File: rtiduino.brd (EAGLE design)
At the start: 181.8 x 126 mm, 111 parts, among them IC7 LM358D, J1 DCJ0202, J2 3.5MM-JACK, J3 2.5MM-JACK, Q2 16MHz, T1 NDT2955, T2 FDN340P, U1 ATMEGA2560AU, U10 AQV252G, U11 AQV252G, U12 AQV252G, U13 AQV252G, U14 AQV252G, U15 AQV252G, U16 AQV252G, U17 AQV252G, U2 LDU240S500, U20 AQV252G, U21 AQV252G, U22 AQV252G, U23 AQV252G, U24 AQV252G, U25 AQV252G, U26 AQV252G, U27 AQV252G, U3 LM2594HVM-3.3, U30 AQV252G, U31 AQV252G, U32 AQV252G, U33 AQV252G, U34 AQV252G, U35 AQV252G, U36 AQV252G, U37 AQV252G, U4 FT232RL, U5 FOD852

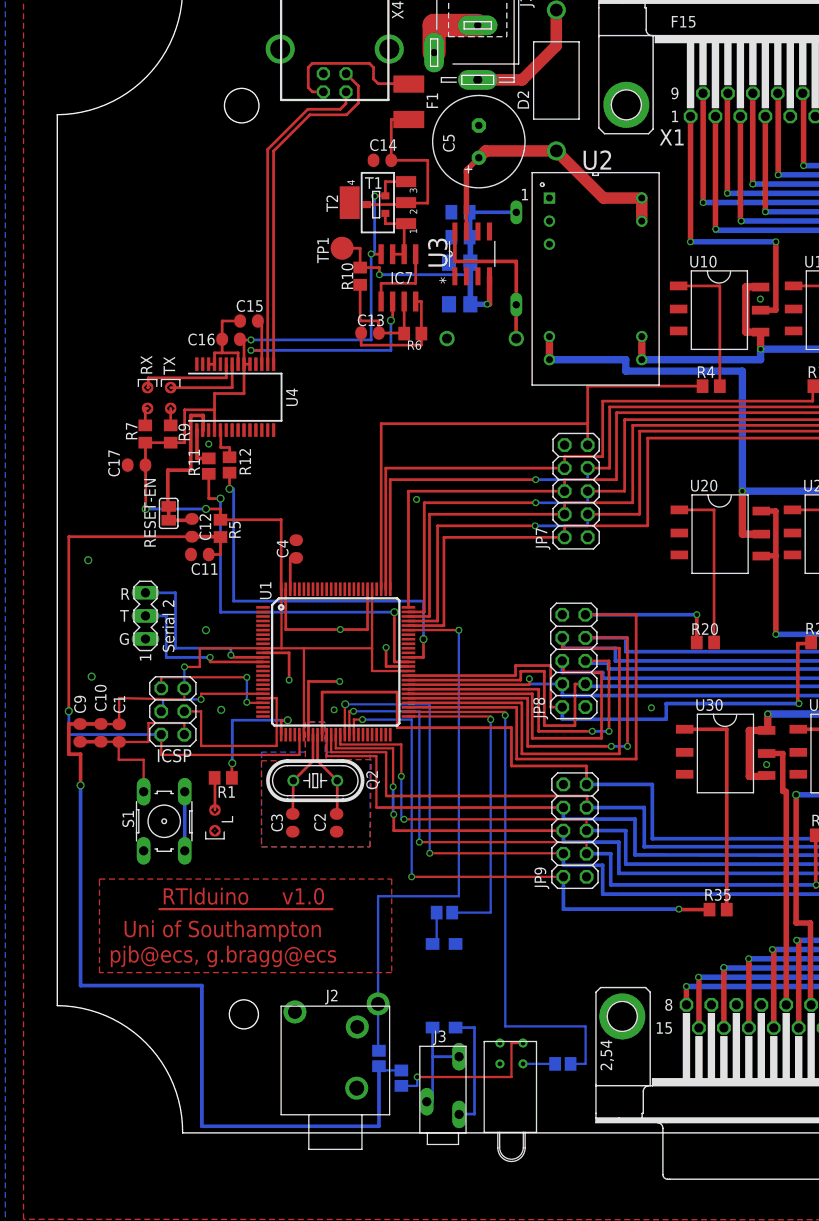
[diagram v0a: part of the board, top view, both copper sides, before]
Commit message: Latest version with * fixed PSU arrangement * more caps * connectors moved outwards
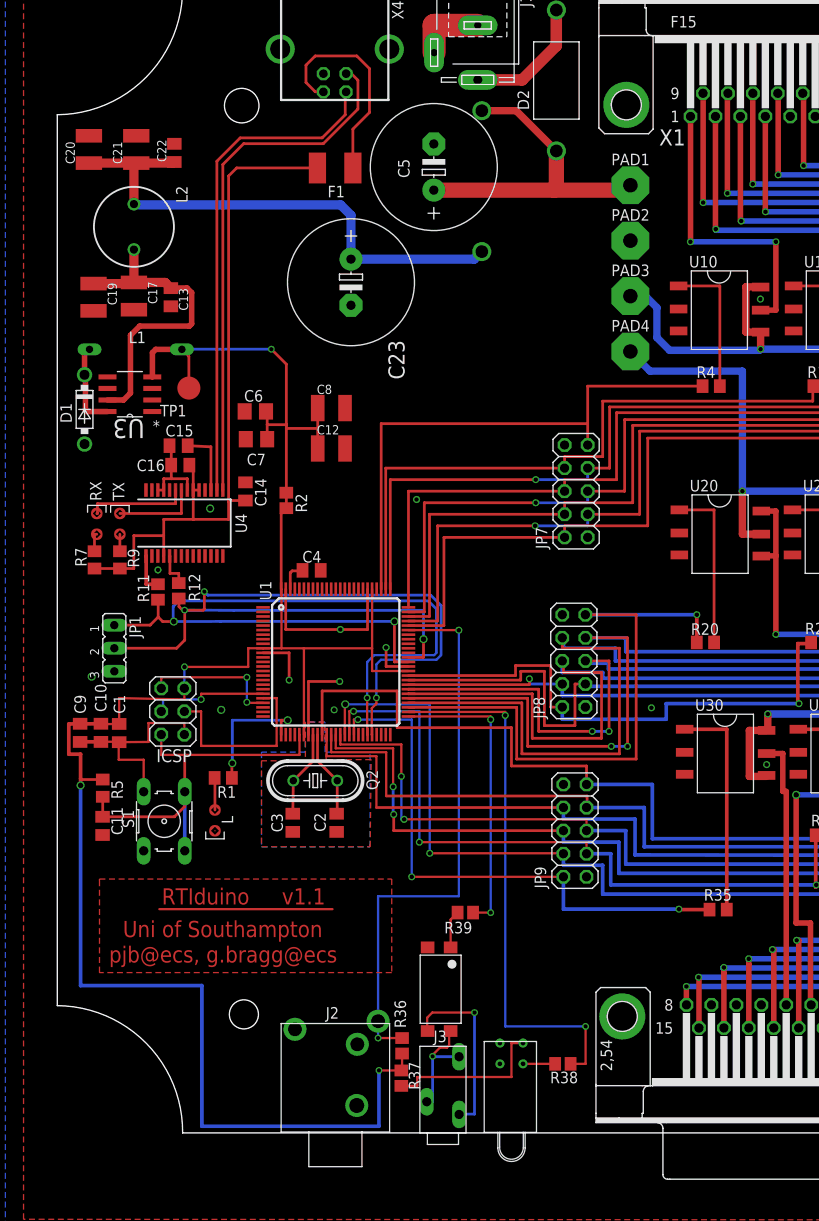
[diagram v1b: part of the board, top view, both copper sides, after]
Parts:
- removed C18: (no value), resistor:C0805K
- removed IC7: LM358D, linear:SO08
- removed R10, R6: 10k, rcl:R0805
- removed RESET-EN: (no value), jumper:SJ
- removed SV1: (no value), con-lstb:MA03-1
- removed T1: NDT2955, zetex:SOT223
- removed T2: FDN340P, zetex:SOT-23
- removed U2: LDU240S500, RTI:RELAY_LDU2430S700
- added C19, C20, C21: (no value), resistor:C1210K
- added C22: (no value), rcl:C0805K
- added C23: 68uF, rcl:E5-13
- added D3: SF37, farnell-parts:DO-201AD
- added JP1: (no value), jumper:JP2
- added L2: (no value), rcl:6000-XXXX-RC
- added PAD1: VIN, wirepad:4,16O1,6
- added PAD2: GND, wirepad:4,16O1,6
- added PAD3: LED_VCC, wirepad:4,16O1,6
- added PAD4: LED_GND, wirepad:4,16O1,6
- added R2: 0R, resistor:R0805
- C1, C10, C11, C14, C15, C16, C2, C3, C4, C9: device rcl:C0805RND -> rcl:C0805K
- C12, C17: value 100n -> (none); device rcl:C0805RND -> resistor:C1210K
- C13: value 100n -> (none); device rcl:C0805RND -> rcl:C0805K
- C5: device resistor:E3,5-10 -> rcl:E5-13
- C8: device resistor:C0805K -> resistor:C1210K
- moved D1 44.4 mm to (3.71, 78.1), flipped to the top, turned to 270 degrees
- moved L1 43.0 mm to (9.34, 84.7), turned to 180 degrees
- moved U3 40.7 mm to (8.70, 79.8), turned to 180 degrees
- moved C14 39.4 mm to (21.4, 69.1), turned to 90 degrees
- moved C11 31.7 mm to (5.69, 32.3), turned to 270 degrees
- moved R5 31.4 mm to (5.71, 36.4)
- moved C7 29.6 mm to (22.6, 74.8), flipped to the top, turned to 0 degrees
- moved C6 25.4 mm to (22.5, 77.9), flipped to the top, turned to 0 degrees
- moved C8 23.6 mm to (30.9, 78.2), flipped to the top
- moved TP1 22.8 mm to (15.2, 80.4), turned to 90 degrees
- moved C13 22.3 mm to (13.2, 90.4), turned to 270 degrees
- moved C17 18.6 mm to (9.14, 90.6), turned to 270 degrees
- moved C12 17.6 mm to (30.9, 73.8), turned to 0 degrees
- moved C15 15.8 mm to (14.1, 74.1)
- moved C16 14.9 mm to (14.2, 72.0)
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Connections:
- removed net 5VREG: C18.1, C6.+, C7.+, C8.1, L1.2, R10.2, TP1.TP, U3.4
- removed net CMP: C13.2, IC7.3, R10.1, R6.2
- removed net DTR: C12.1, RESET-EN.1, RESET-EN.2, U4.2
- removed net GATE_CMD: IC7.6, IC7.7, T1.1, T2.3
- removed net RXD3: R11.2, U1.63
- removed net TXD3: R12.2, U1.64
- new net RXD: JP1.1, R11.2, U1.45, U1.63
- new net TXD: JP1.2, R12.2, U1.46, U1.64
- net +3V3: no longer IC7.2
- net +5V: now also C12.1, C6.+, C7.+, C8.1, L1.2, R2.1, R2.2, TP1.TP, U3.4; no longer C16.1, C17.2, IC7.8, R7.2, R9.2, T1.3, T2.2, U4.19, U4.20, U4.4
- net GND: now also C12.2, C13.2, C17.2, C19.2, C20.2, C21.2, C22.2, C23.-, JP1.3, PAD2.1; no longer C13.1, C17.1, C18.2, IC7.4, R6.1, SV1.1, U2.1, U2.2
- net LED_GND: now also PAD4.1; no longer U2.7, U2.8
- net LED_VCC: now also PAD3.1; no longer U2.10, U2.9
- net N$4: now also C20.1, C21.1, C22.1, C23.+, D3.1, L2.1; no longer IC7.1, IC7.5
- net N$43: now also C13.1, C17.1, C19.1, L2.2, U3.7; no longer S1.3, S1.4
- net RESET: now also S1.3, S1.4; no longer C12.2
- net RXD2: no longer SV1.3
- net TXD2: no longer SV1.2
- net USBVCC: now also C16.1, R7.2, R9.2, U4.19, U4.20, U4.4; no longer T1.2, T2.1
- net VIN: now also D3.2, PAD1.1; no longer U2.15, U2.16, U3.7
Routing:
- net TXD: track 0.00 -> 98.0 mm, vias 0 -> 4
- net RXD: track 0.00 -> 91.4 mm, vias 0 -> 3
- net USBVCC: track 21.9 -> 79.3 mm
- net N$4: track 9.01 -> 58.0 mm
- net TXD3: track 43.3 -> 0.00 mm, vias 2 -> 0
- net RXD3: track 42.7 -> 0.00 mm, vias 2 -> 0
- net 5VREG: track 37.9 -> 0.00 mm, vias 2 -> 0
- net +5V: track 251.9 -> 223.2 mm, vias 7 -> 4
- net N$43: track 6.50 -> 34.8 mm
- net RESET: track 71.6 -> 43.6 mm, vias 1 -> 0
- net RXD2: track 20.0 -> 0.00 mm, vias 1 -> 0
- net +3V3: track 27.3 -> 7.32 mm, vias 2 -> 0
- net DTR: track 19.9 -> 0.00 mm
- net D-: track 35.6 -> 55.0 mm
- net D+: track 38.7 -> 58.0 mm
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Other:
- board text added: "v1.1"
- board text removed: "G"
- board text removed: "R"
- board text removed: "Serial 2"
- board text removed: "T"
- board text removed: "v1.0"

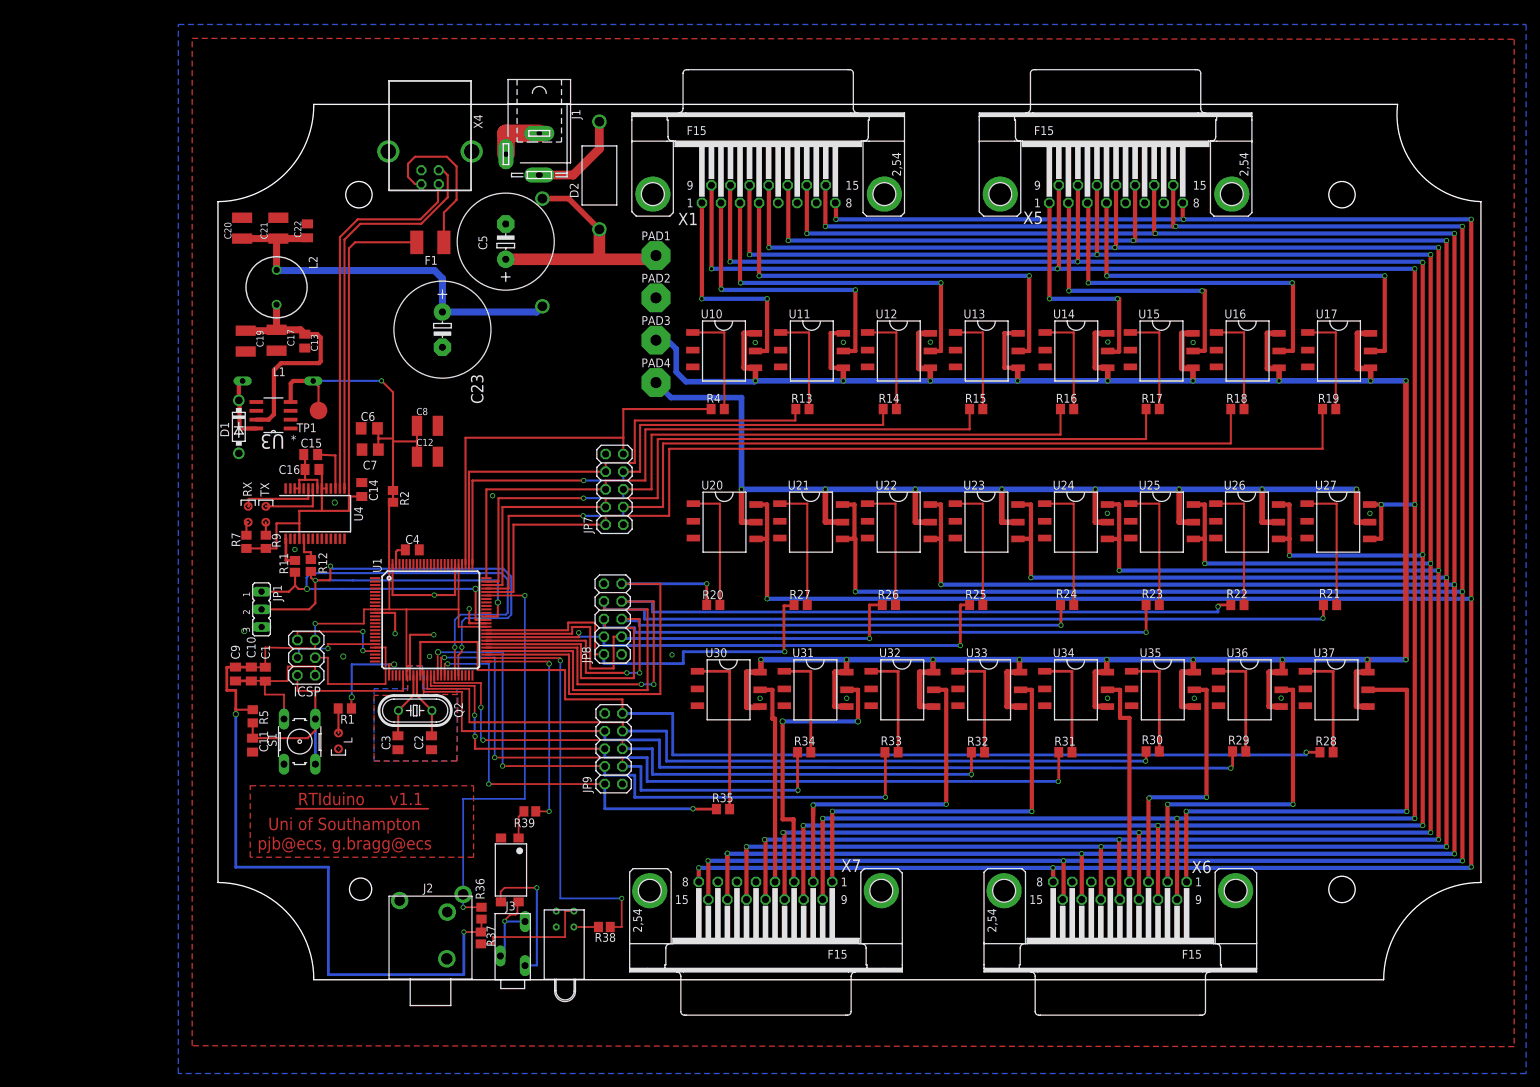
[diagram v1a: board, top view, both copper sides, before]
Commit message: Update wih Superdome PCB
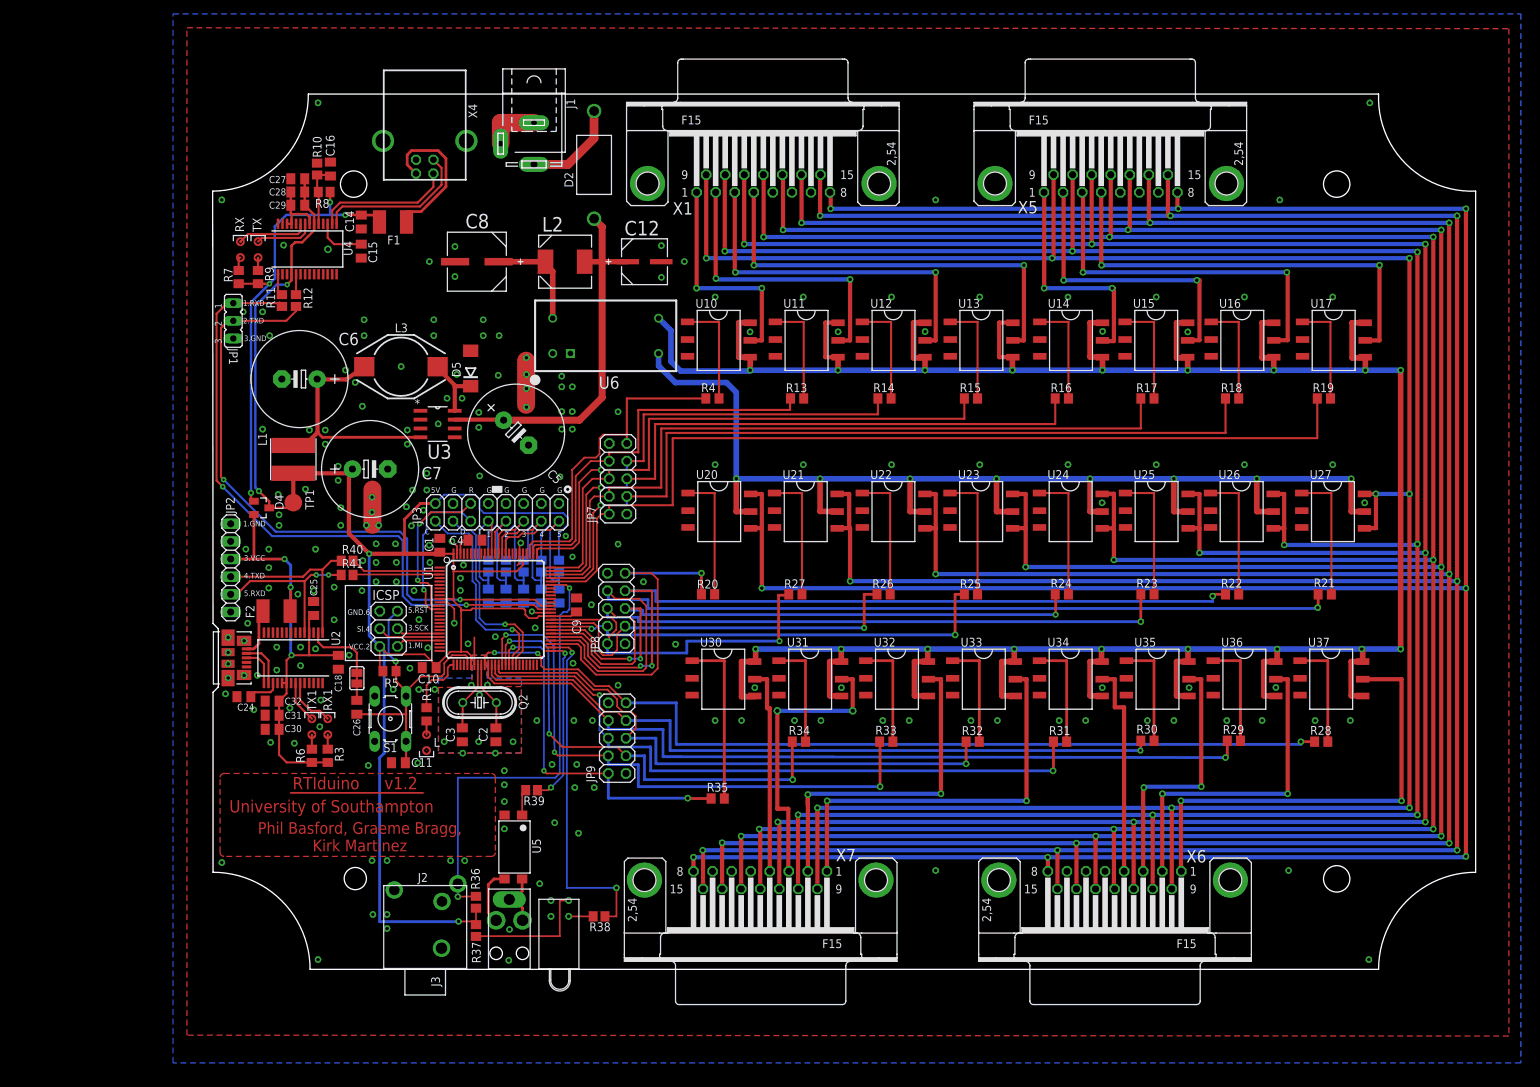
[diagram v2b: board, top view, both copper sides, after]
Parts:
- removed C13, C22: (no value), rcl:C0805K
- removed C17, C19, C20, C21: (no value), resistor:C1210K
- removed C23: 68uF, rcl:E5-13
- removed D1: 1N5817-B, diode:DO41-7.6
- removed D3: SF37, farnell-parts:DO-201AD
- removed PAD1: VIN, wirepad:4,16O1,6
- removed PAD2: GND, wirepad:4,16O1,6
- removed PAD3: LED_VCC, wirepad:4,16O1,6
- removed PAD4: LED_GND, wirepad:4,16O1,6
- removed R2: 0R, resistor:R0805
- added C18, C24, C25, C26, C27, C28, C30, C31: 100nF, rcl:C0805K
- added C29, C32: 4.7uF, rcl:C0805K
- added C42, C43, C44, C45, C46: 100n, rcl:C0805K
- added D4: BAT54C, diode:SOT23
- added D5: MBRS130, diode:DO214AA
- added F2: 500mA, rcl:L1812
- added J4: USB PROG, CC11x:MOLEX_47346-0001
- added JP2: (no value), pinhead:1X06
- added JP3: (no value), pinhead:2X08
- added L3: 330uH (DO3308P-334), inductor-coilcraft:DO3316P
- added R10: 10K, resistor:R0805
- added R3, R6: 1k, rcl:R0805
- added R40, R41: 1K, resistor:R0805
- added R42, R43, R44, R45, R46: 10k, resistor:R0805
- added R8: 4K7, resistor:R0805
- added RESET-EN: (no value), jumper:SJ
- added RX1, TX1: (no value), led:0805RND
- added U2: FT232RL, SmartPrj:SSOP28
- added U6: LED-DRIVER, RTI:LDU08
- C12: value (none) -> 10UF; device resistor:C1210K -> RTI:CAPAE660X610N
- C6: device resistor:R/2012-12R -> rcl:E5-13
- C7: value 68uF -> 100uF; device resistor:R/2012-12R -> rcl:E5-13
- C8: value (none) -> 47UF; device resistor:C1210K -> RTI:CAPAE830X1050N
- J3: value 2.5MM-JACK -> 2.5MM-JACKPRO; device RTI:2.5-JACK-RA -> RTI:2.5-JACK-RA-PRO
- L1: value 100uH -> 3uH; device inductors:SBC10 -> RTI:WE-TPC_5818/5828
- L2: value (none) -> DR73-680-R; device rcl:6000-XXXX-RC -> RTI:INDM7676X355N
- U3: value LM2594HVM-3.3 -> LM2594HVM-5.0
- moved C9 50.1 mm to (52.3, 52.5), turned to 90 degrees
- moved C16 43.3 mm to (16.9, 115.2), turned to 270 degrees
- moved C12 42.0 mm to (62.1, 101.9)
- moved JP1 41.7 mm to (2.92, 93.3)
- moved L2 41.7 mm to (50.7, 101.9), turned to 0 degrees
- moved C14 38.5 mm to (21.3, 107.6), turned to 270 degrees
- moved R11 38.3 mm to (9.91, 96.3)
- moved R12 38.2 mm to (11.9, 96.3)
- moved RX 38.1 mm to (3.94, 103.6)
- moved TX 38.1 mm to (6.48, 103.6)
- moved U4 38.1 mm to (13.6, 103.7)
- moved R7 38.1 mm to (3.69, 99.6)
- moved R9 38.1 mm to (6.48, 99.6)
- moved C1 31.2 mm to (32.6, 61.0), turned to 90 degrees
- moved C15 30.2 mm to (21.3, 103.4), turned to 90 degrees
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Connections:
- new net +3V3PROG: C24.2, U2.17
- new net N$50: RX1.P$2, U2.23
- new net N$52: TX1.P$2, U2.22
- new net N$58: R3.1, RX1.P$1
- new net N$62: R6.1, TX1.P$1
- new net N$63: F2.2, J4.1
- new net N$66: C26.1, RESET-EN.1, RESET-EN.2, U2.2
- new net N$68: C16.2, R10.1, R8.2, U4.19
- new net PROG_D+: J4.3, U2.15
- new net PROG_D-: J4.2, U2.16
- new net RXD1: U1.45
- new net RXDP: JP2.4, R40.1, U2.1
- new net RXD_PROG: R40.2, U1.2
- new net SCL: JP3.1, U1.43
- new net SDA: JP3.3, U1.44
- new net SW1: C46.1, JP3.7, R46.2, U1.89
- new net SW2: C45.1, JP3.9, R45.2, U1.88
- new net SW3: C44.1, JP3.11, R44.2, U1.87
- new net SW4: C43.1, JP3.13, R43.2, U1.86
- new net SW5: C42.1, JP3.15, R42.2, U1.85
- new net TXD1: U1.46
- new net TXDP: JP2.5, R41.1, U2.5
- new net TXD_PROG: R41.2, U1.3
- new net USBPROGVCC: C18.1, C25.1, C30.1, C31.1, C32.1, D4.2, F2.1, JP2.3, R3.2, R6.2, U2.19, U2.20, U2.4
- net +5V: now also C27.1, C28.1, C29.1, D4.3, JP3.2, R42.1, R43.1, R44.1, R45.1, R46.1, U4.20, U4.4; no longer C12.1, C6.+, C8.1, R2.1, R2.2, U3.4
- net GND: now also C16.1, C18.2, C24.1, C25.2, C27.2, C28.2, C29.2, C30.2, C31.2, C32.2, C42.2, C43.2, C44.2, C45.2, C46.2, D5.A, J4.5, J4.M1, J4.M2, J4.M3, J4.M4, J4.M5, J4.M6, JP2.1, JP3.10, JP3.12, JP3.14, JP3.16, JP3.4, JP3.8, R10.2, U2.18, U2.21, U2.25, U2.26, U2.7, U6.1; no longer C13.2, C16.2, C17.2, C19.2, C20.2, C21.2, C22.2, C23.-, D1.A, PAD2.1
- net LED_GND: now also U6.7; no longer PAD4.1
- net LED_VCC: now also U6.8; no longer PAD3.1
- net N$4: now also C6.+, L1.1, L3.2, U3.4; no longer C20.1, C21.1, C22.1, C23.+, D3.1, L2.1
- net N$43: now also C8.1, L2.1, U6.14; no longer C13.1, C17.1, C19.1, L2.2, U3.7
- net N$48: now also D5.C, L3.1; no longer D1.C, L1.1
- net N$51: now also J3.R, J3.T; no longer J3.2, J3.3
- net N$61: now also J3.S; no longer J3.1
- net RESET: now also C26.2
- net RXD: no longer U1.45
- net RXD2: now also JP3.6
- net TXD: no longer U1.46
- net TXD2: now also JP3.5
- net USBVCC: now also D4.1, R8.1; no longer C16.1, U4.19, U4.20, U4.4
- net VIN: now also C12.1, L2.2, U3.7; no longer D3.2, PAD1.1
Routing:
- net +5V: track 223.2 -> 302.0 mm
- net USBPROGVCC: track 0.00 -> 68.2 mm, vias 0 -> 3
- net D+: track 58.0 -> 22.5 mm
- net D-: track 55.0 -> 19.8 mm
- net SCL: track 0.00 -> 30.3 mm, vias 0 -> 1
- net SDA: track 0.00 -> 28.4 mm, vias 0 -> 1
- net RXDP: track 0.00 -> 25.9 mm
- net TXDP: track 0.00 -> 24.5 mm, vias 0 -> 2
- net N$4: track 58.0 -> 34.5 mm
- net SW5: track 0.00 -> 23.3 mm
- net RXD2: track 0.00 -> 23.0 mm, vias 0 -> 2
- net GND: track 78.6 -> 56.0 mm, vias 23 -> 219
- net TXD2: track 0.00 -> 22.4 mm, vias 0 -> 1
- net SW4: track 0.00 -> 21.5 mm
- net C0: track 150.9 -> 131.0 mm, vias 1 -> 3
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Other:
- outline, holes or cut-outs redrawn
- board text added: "1"
- board text added: "1.GND"
- board text added: "1.MI"
- board text added: "1.RXD"
- board text added: "2"
- board text added: "2.TXD"
- board text added: "3"
- board text added: "3.GND"
- board text added: "3.SCK"
- board text added: "3.VCC"
- board text added: "4"
- board text added: "4.TXD"
- board text added: "5"
- board text added: "5.!RST"
- board text added: "5.RXD"
- board text added: "5V"
- board text added: "C"
- board text added: "D"
- board text added: "G"
- board text added: "GND.6"
- board text added: "Phil Basford, Graeme Bragg, Kirk Martinez"
- board text added: "R"
- board text added: "SI.4"
- board text added: "T"
- board text added: "University of Southampton"
- board text added: "VCC.2"
- board text added: "v1.2"
- board text removed: "Uni of Southampton"
- board text removed: "pjb@ecs, g.bragg@ecs"
- board text removed: "v1.1"
